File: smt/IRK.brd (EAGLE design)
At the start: 142.9 x 39.7 mm, 41 parts, among them IC1 PIC18F25K50, IC2 MAX4066ESD, Q1 MMBT2222A, Q2 MMBT3906, U1 TSOP4838

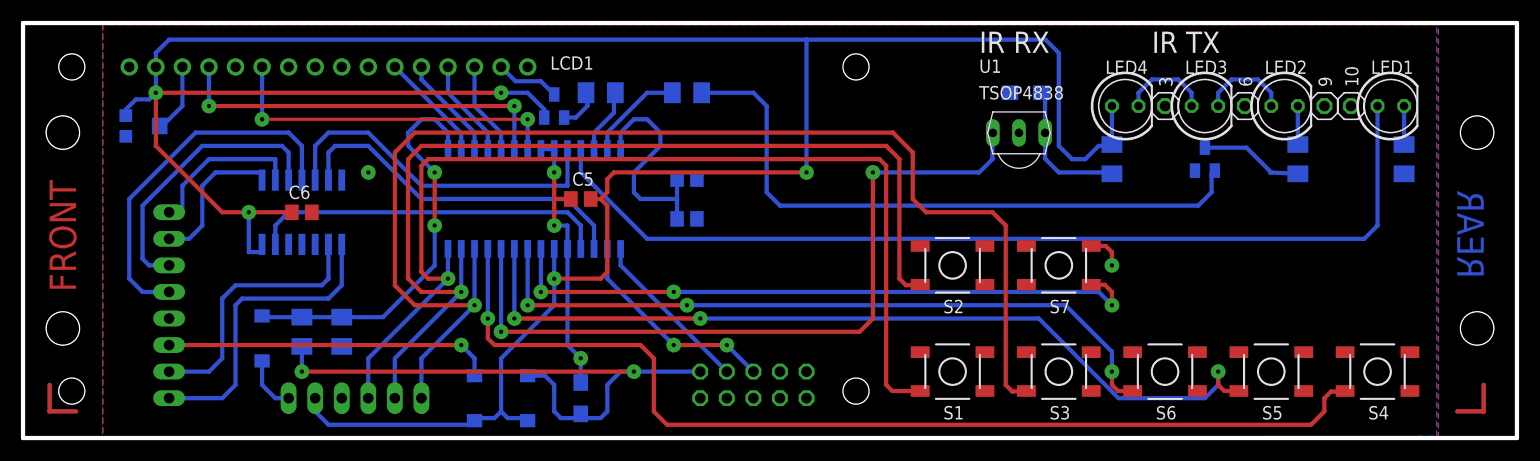
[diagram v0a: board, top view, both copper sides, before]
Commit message: Updated the LCD package to have 3 mm mounting holes.
The original ones were 2.5 mm but didn't match reality.
So I had to drill out the mounting holes to 3 mm (or else
find 2.5 mm bolts which are quite hard to find). M3 bolts
are much more commonly available. Had to reroute one of the
PCB traces to avoid a hole as a result.
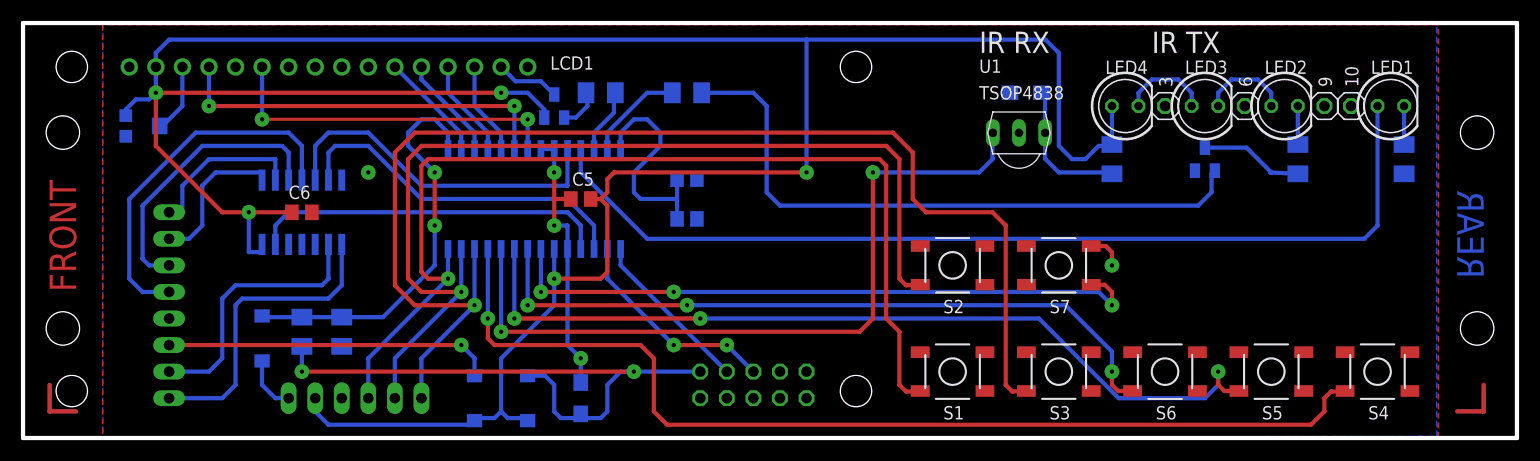
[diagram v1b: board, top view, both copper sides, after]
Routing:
- net N$12: track 99.8 -> 99.1 mm
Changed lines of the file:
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@@
 <grid distance="0.05" unitdist="inch" unit="inch" style="lines" multiple="1" display="yes" altdistance="0.025" altunitdist="inch" altunit="inch"/>
 <layers>
-<layer number="1" name="Top" color="11" fill="1" visible="no" active="yes"/>
+<layer number="1" name="Top" color="11" fill="1" visible="yes" active="yes"/>
 <layer number="2" name="Route2" color="1" fill="3" visible="no" active="no"/>
 <layer number="3" name="Route3" color="4" fill="3" visible="no" active="no"/>
@@
 <wire x1="40.64" y1="15.24" x2="33.02" y2="7.62" width="0.4064" layer="16"/>
 <via x="40.64" y="15.24" extent="1-16" drill="0.4064"/>
-<wire x1="82.55" y1="5.08" x2="82.55" y2="26.035" width="0.4064" layer="1"/>
+<wire x1="82.55" y1="11.43" x2="82.55" y2="26.035" width="0.4064" layer="1"/>
 <wire x1="82.55" y1="26.035" x2="81.915" y2="26.67" width="0.4064" layer="1"/>
 <wire x1="81.915" y1="26.67" x2="38.735" y2="26.67" width="0.4064" layer="1"/>
@@
 <wire x1="38.1" y1="15.875" x2="38.735" y2="15.24" width="0.4064" layer="1"/>
 <wire x1="38.735" y1="15.24" x2="40.64" y2="15.24" width="0.4064" layer="1"/>
-<wire x1="85.8012" y1="4.4958" x2="83.1342" y2="4.4958" width="0.4064" layer="1"/>
-<wire x1="83.1342" y1="4.4958" x2="82.55" y2="5.08" width="0.4064" layer="1"/>
 <contactref element="IC1" pad="28"/>
 <wire x1="40.64" y1="18.08" x2="40.64" y2="15.24" width="0.4064" layer="16"/>
+<wire x1="82.55" y1="11.43" x2="83.82" y2="10.16" width="0.4064" layer="1"/>
+<wire x1="83.82" y1="10.16" x2="83.82" y2="5.08" width="0.4064" layer="1"/>
+<wire x1="83.82" y1="5.08" x2="84.455" y2="4.445" width="0.4064" layer="1"/>
+<wire x1="84.455" y1="4.445" x2="85.7504" y2="4.445" width="0.4064" layer="1"/>
+<wire x1="85.7504" y1="4.445" x2="85.8012" y2="4.4958" width="0.4064" layer="1"/>
 </signal>
 <signal name="N$13">
